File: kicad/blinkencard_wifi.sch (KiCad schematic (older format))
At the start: 1 part, among them U2 ESP32-WROOM-32D

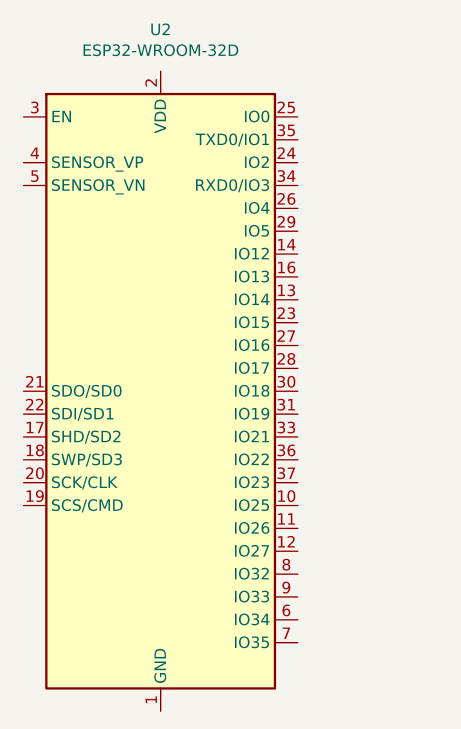
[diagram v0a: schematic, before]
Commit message: Start routing LEDs. Start ESP32 integration
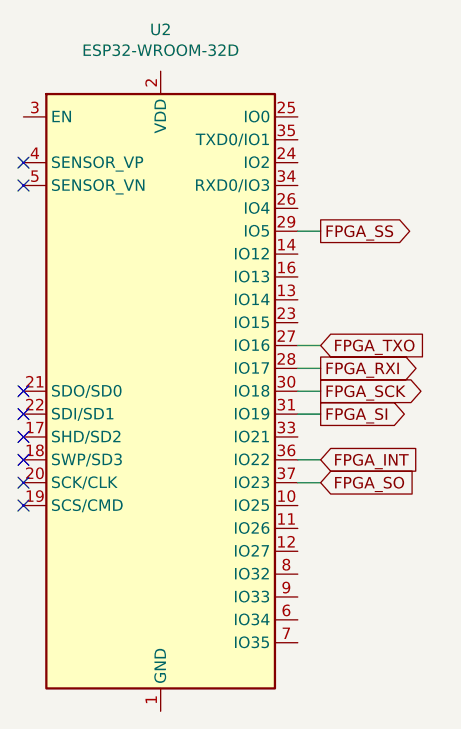
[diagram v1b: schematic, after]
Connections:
- net FPGA_TXO: now reaches U2.27 (IO16)
- net FPGA_RXI: now reaches U2.28 (IO17)
- net FPGA_SS: now reaches U2.29 (IO5)
- net FPGA_SCK: now reaches U2.30 (IO18)
- net FPGA_SI: now reaches U2.31 (IO19)
- net FPGA_INT: now reaches U2.36 (IO22)
- net FPGA_SO: now reaches U2.37 (IO23)
- no-connect marks 0 -> 8
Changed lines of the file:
@@
 	1    0    0    -1
 $EndComp
+Text GLabel 4350 3000 2    50   Output ~ 0
+FPGA_SCK
+Text GLabel 4350 3100 2    50   Output ~ 0
+FPGA_SI
+Text GLabel 4350 3400 2    50   Input ~ 0
+FPGA_SO
+Text GLabel 4350 2300 2    50   Output ~ 0
+FPGA_SS
+Text GLabel 4350 3300 2    50   Input ~ 0
+FPGA_INT
+Wire Wire Line
+	4350 2300 4250 2300
+Wire Wire Line
+	4350 3000 4250 3000
+Wire Wire Line
+	4350 3100 4250 3100
+Wire Wire Line
+	4350 3400 4250 3400
+Wire Wire Line
+	4350 3300 4250 3300
+Text GLabel 4350 2800 2    50   Input ~ 0
+FPGA_TXO
+Text GLabel 4350 2900 2    50   Output ~ 0
+FPGA_RXI
+Wire Wire Line
+	4350 2800 4250 2800
+Wire Wire Line
+	4350 2900 4250 2900
+NoConn ~ 3050 3000
+NoConn ~ 3050 3100
+NoConn ~ 3050 3200
+NoConn ~ 3050 3300
+NoConn ~ 3050 3400
+NoConn ~ 3050 3500
+NoConn ~ 3050 2000
+NoConn ~ 3050 2100
 $EndSCHEMATC
